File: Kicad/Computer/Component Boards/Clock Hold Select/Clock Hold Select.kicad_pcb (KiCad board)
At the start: 2 copper layers, 26.7 x 59.7 mm, 23 parts, among them IC1 AP7365-33WG-7, IC2 74LVC244APW,118, IC3 74LVC32APW,118, IC4 74LVC244APW,118, IC5 74LVC244APW,118, IC6 74LVC32APW,118, J1 Conn_02x20_Counter_Clockwise

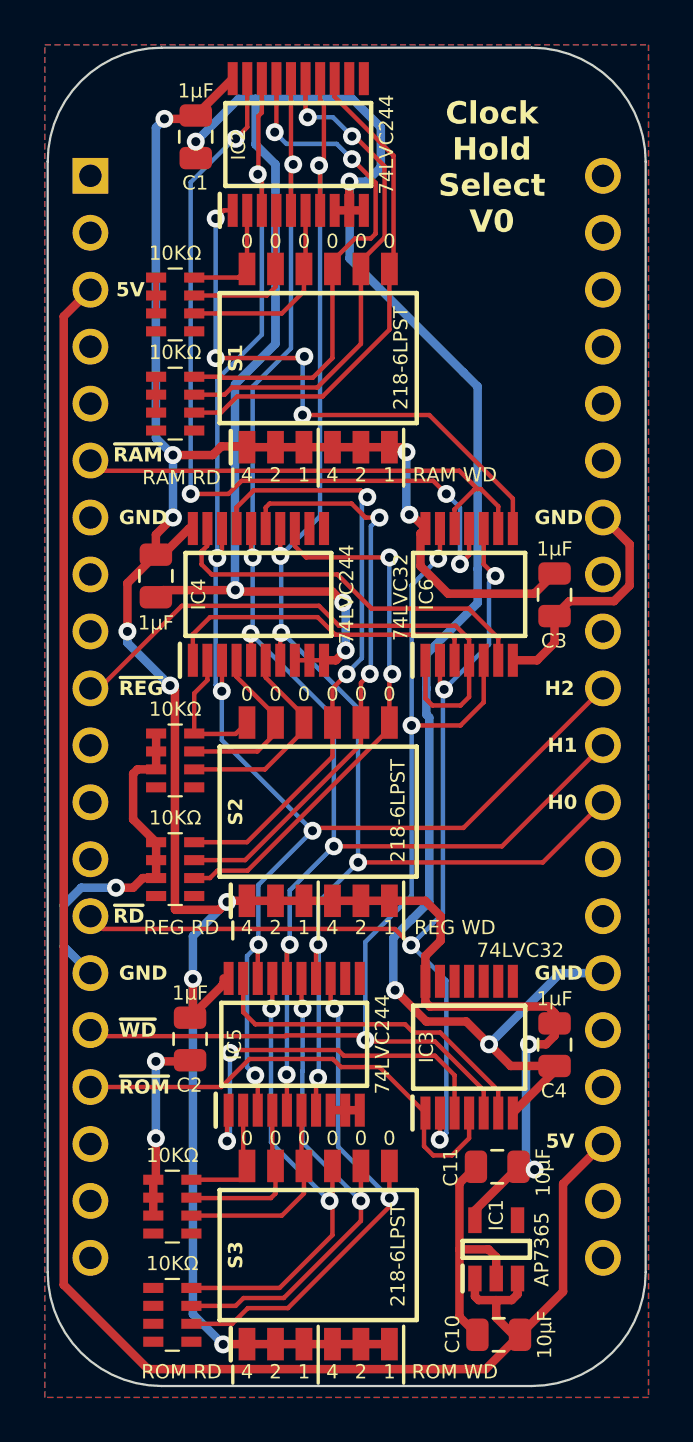
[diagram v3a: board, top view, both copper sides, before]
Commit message: Standardising DIP board layouts.
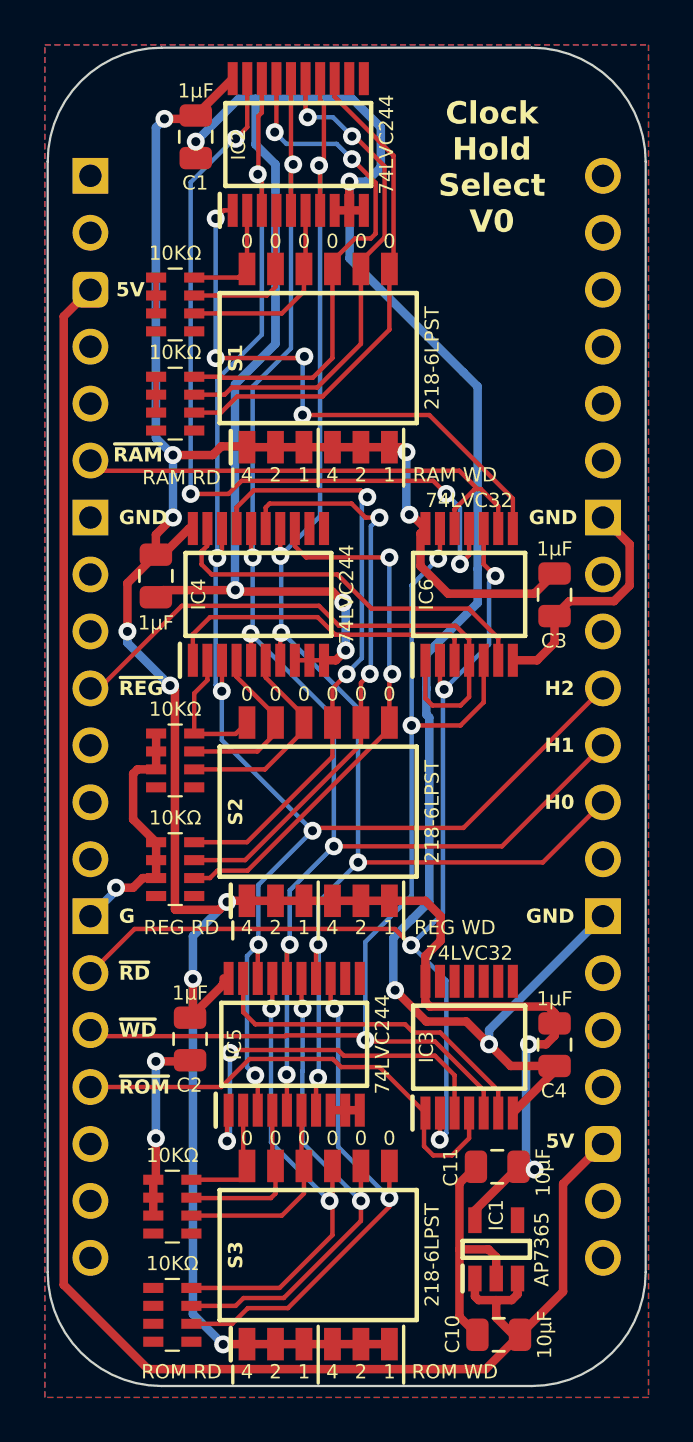
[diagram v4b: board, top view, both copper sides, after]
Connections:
- J1 pad 14: /~{RD} -> /GND
- J1 pad 15: /GND -> /~{RD}
- J1 pad 26: /GND -> unconnected-(J1-Pin_26-Pad26)
- J1 pad 27: unconnected-(J1-Pin_27-Pad27) -> /GND
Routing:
- net /GND: track 160.9 -> 157.9 mm
- net /~{RD}: track 47.2 -> 47.8 mm
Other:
- board text added: "G"

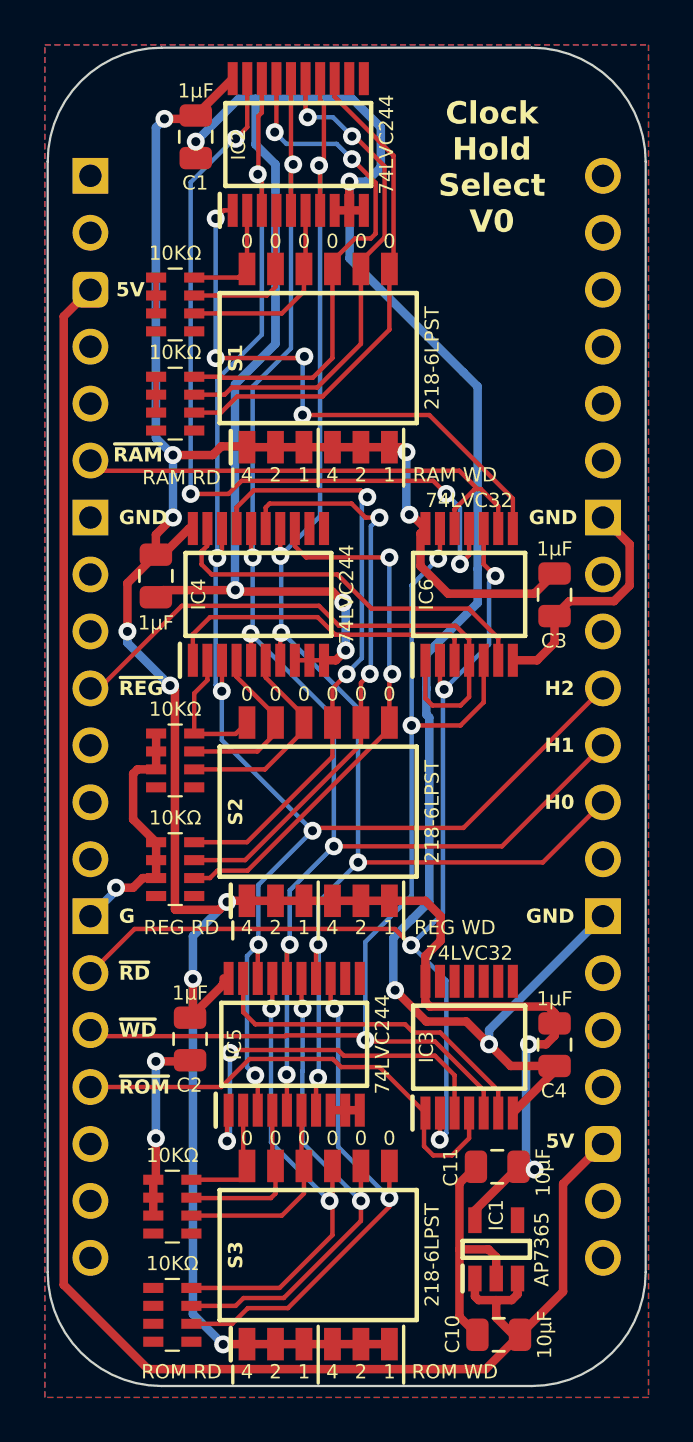
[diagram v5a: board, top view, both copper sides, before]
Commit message: Regenerating some gerbers again with paste layers.
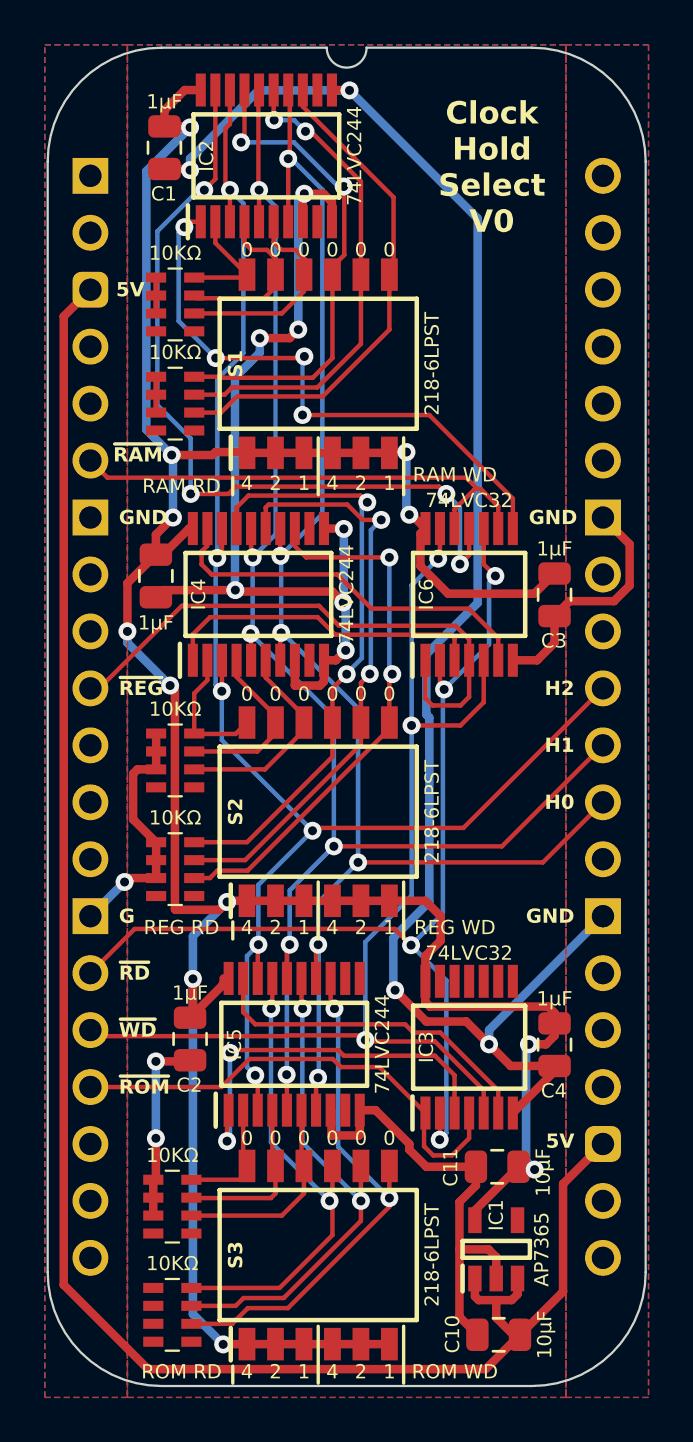
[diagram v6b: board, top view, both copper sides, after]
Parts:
- moved IC2 1.51 mm to (96.7, 57.5)
- moved C1 1.48 mm to (92.2, 57.1)
- moved S1 0.25 mm to (99.1, 66.8)
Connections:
- IC2 pad 11: unconnected-(IC2-2A3-Pad11) -> /GND
- IC2 pad 9: /GND -> unconnected-(IC2-2Y3-Pad9)
- IC4 pad 11: unconnected-(IC4-2A3-Pad11) -> /GND
- IC4 pad 9: /GND -> unconnected-(IC4-2Y3-Pad9)
- IC5 pad 11: unconnected-(IC5-2A3-Pad11) -> /GND
- IC5 pad 9: /GND -> unconnected-(IC5-2Y3-Pad9)
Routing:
- net /GND: track 157.9 -> 171.5 mm, vias 10 -> 14
- net /H1: track 69.3 -> 68.0 mm
- net /RAM WD H2: track 23.1 -> 21.9 mm
- net /RAM WD H1: track 22.5 -> 21.6 mm
- net /H2: track 71.8 -> 70.9 mm
- net /H0: track 67.2 -> 68.1 mm
- net /RAM RD H1: track 7.15 -> 6.48 mm
- net /3.3V: track 133.2 -> 133.7 mm
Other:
- outline, holes or cut-outs redrawn
